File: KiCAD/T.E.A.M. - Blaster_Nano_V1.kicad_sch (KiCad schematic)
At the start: 47 parts, among them J1 USB_C_Receptacle_USB2.0_14P, J2 Conn_01x02, J3 LED, J4 Taster, J5 Speaker, J6 Conn_02x03_Counter_Clockwise, Q1 FS8205A, U1 TP4056-42-ESOP8, U2 DW01A, U3 MT3608, U4 ATMEGA328P-AU, U5 CH340G, U6 DFR0299, Y1 16MHz, Y2 12MHz

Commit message: BOM erstellt und heruntergeladen.
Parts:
- Q1: Availability In Stock -> (none); Package Package -> (none); Price None -> (none)
- U4: Availability In Stock -> (none); Package TQFP-32 Microchip -> (none); Price None -> (none)
- U6: Availability In Stock -> (none); Package None -> (none); Price None -> (none)
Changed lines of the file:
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@@
 			)
 		)
-		(property "Package" "Package"
-			(at 77.47 107.95 0)
-			(hide yes)
-			(show_name no)
-			(do_not_autoplace no)
-			(effects
-				(font
-					(size 1.27 1.27)
-				)
-				(justify bottom)
-			)
-		)
-		(property "Price" "None"
-			(at 77.47 107.95 0)
-			(hide yes)
-			(show_name no)
-			(do_not_autoplace no)
-			(effects
-				(font
-					(size 1.27 1.27)
-				)
-				(justify bottom)
-			)
-		)
 		(property "Check_prices" "https://www.snapeda.com/parts/FS8205A/Fortune+Semiconductor/view-part/?ref=eda"
 			(at 77.47 107.95 0)
@@
 			)
 		)
-		(property "Availability" "In Stock"
-			(at 77.47 107.95 0)
-			(hide yes)
-			(show_name no)
-			(do_not_autoplace no)
-			(effects
-				(font
-					(size 1.27 1.27)
-				)
-				(justify bottom)
-			)
-		)
 		(property "MANUFACTURER" "Fortune Semiconductor"
 			(at 77.47 107.95 0)
@@
 			)
 		)
-		(property "Package" "TQFP-32 Microchip"
-			(at 187.96 55.88 0)
-			(hide yes)
-			(show_name no)
-			(do_not_autoplace no)
-			(effects
-				(font
-					(size 1.27 1.27)
-				)
-				(justify bottom)
-			)
-		)
-		(property "Price" "None"
-			(at 187.96 55.88 0)
-			(hide yes)
-			(show_name no)
-			(do_not_autoplace no)
-			(effects
-				(font
-					(size 1.27 1.27)
-				)
-				(justify bottom)
-			)
-		)
 		(property "Check_prices" "https://www.snapeda.com/parts/ATMEGA328P-AU/Microchip+Technology/view-part/?ref=eda"
 			(at 187.96 55.88 0)
@@
 			)
 		)
-		(property "Availability" "In Stock"
-			(at 187.96 55.88 0)
-			(hide yes)
-			(show_name no)
-			(do_not_autoplace no)
-			(effects
-				(font
-					(size 1.27 1.27)
-				)
-				(justify bottom)
-			)
-		)
 		(property "MANUFACTURER" "Microchip"
 			(at 187.96 55.88 0)
@@
 			)
 		)
-		(property "Package" "None"
-			(at 143.51 135.89 0)
-			(hide yes)
-			(show_name no)
-			(do_not_autoplace no)
-			(effects
-				(font
-					(size 1.27 1.27)
-				)
-				(justify bottom)
-			)
-		)
 		(property "Check_prices" "https://www.snapeda.com/parts/DFR0299/DFRobot/view-part/?ref=eda"
 			(at 143.51 135.89 0)
@@
 			)
 		)
-		(property "Price" "None"
-			(at 143.51 135.89 0)
-			(hide yes)
-			(show_name no)
-			(do_not_autoplace no)
-			(effects
-				(font
-					(size 1.27 1.27)
-				)
-				(justify bottom)
-			)
-		)
 		(property "SnapEDA_Link" "https://www.snapeda.com/parts/DFR0299/DFRobot/view-part/?ref=snap"
 			(at 143.51 135.89 0)
@@
 			(at 143.51 135.89 0)
 			(hide yes)
-			(show_name no)
-			(do_not_autoplace no)
-			(effects
-				(font
-					(size 1.27 1.27)
-				)
-				(justify bottom)
-			)
-		)
-		(property "Availability" "In Stock"
-			(at 143.51 135.89 0)
-			(hide yes)

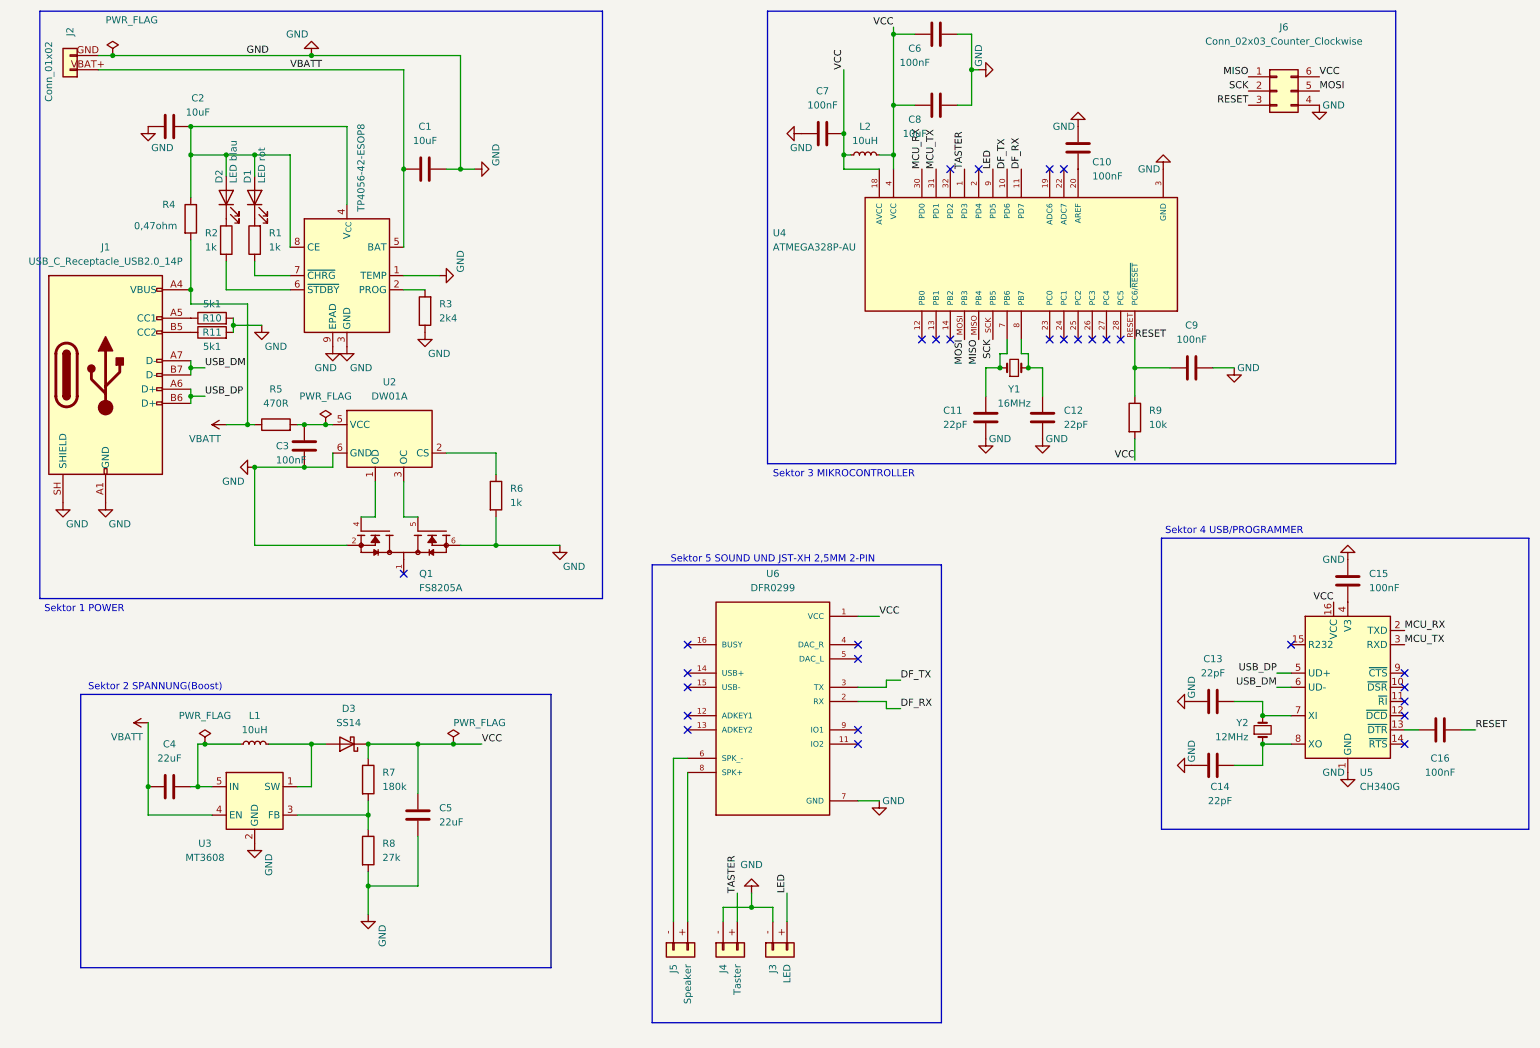
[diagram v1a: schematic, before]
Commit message: Fix schematic pin numbers (J2-J5) and footprint references (Q1, Y1, Y2, U6)
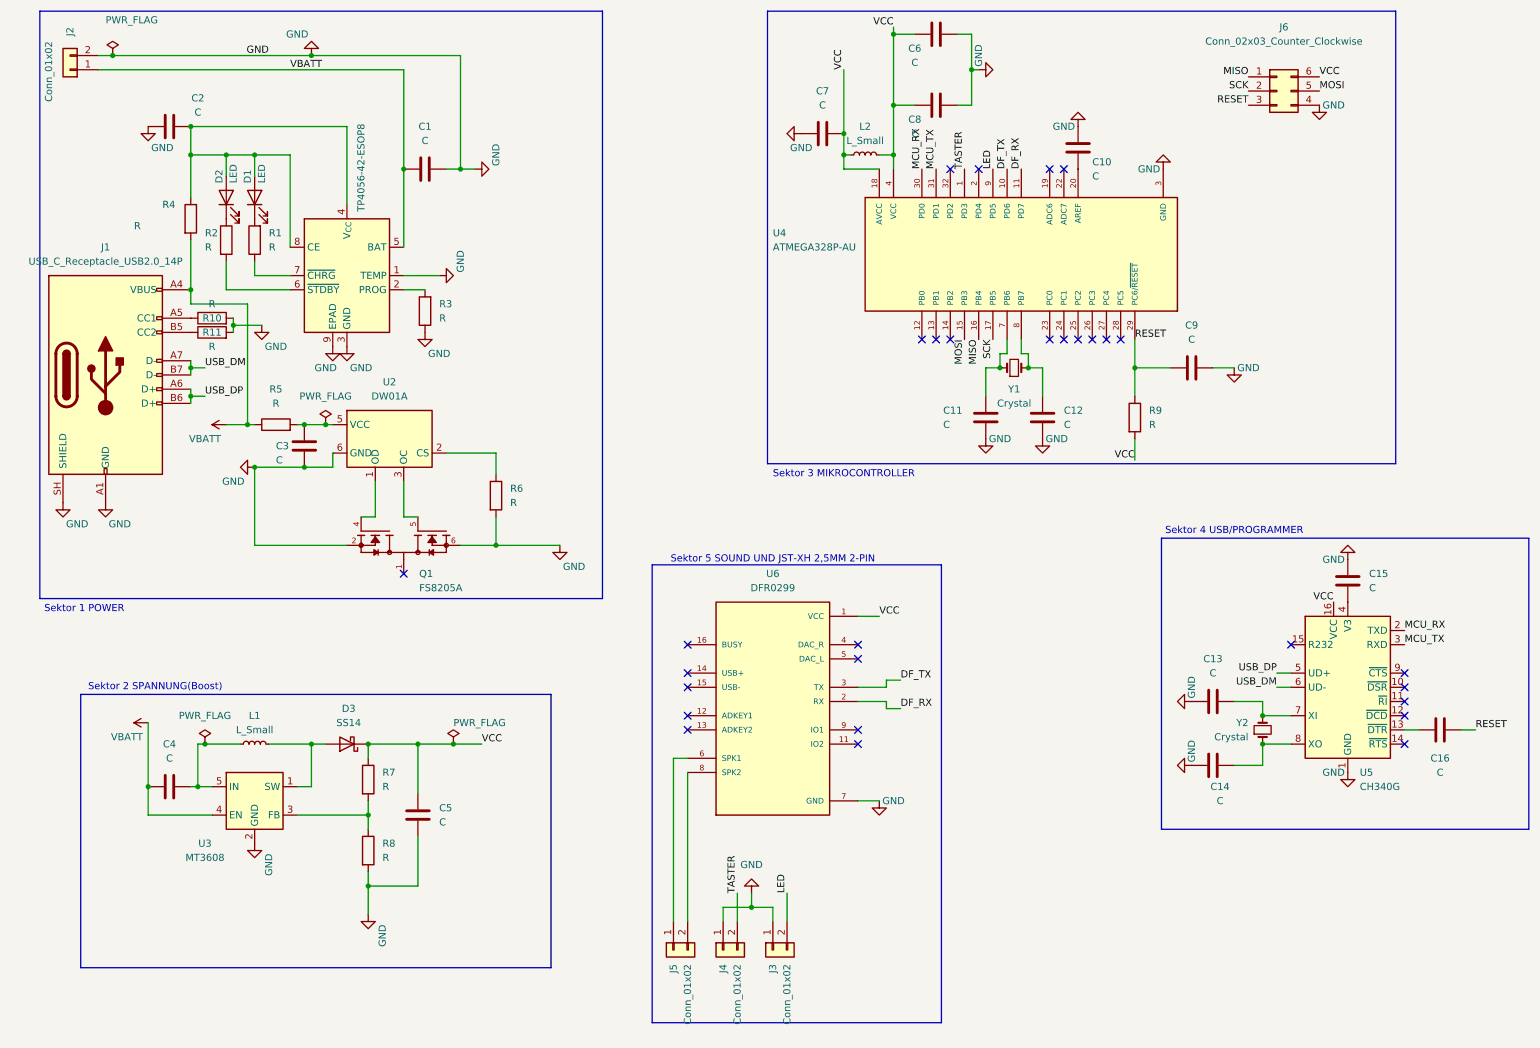
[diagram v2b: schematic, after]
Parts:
- C1, C2, C8: value 10uF -> C
- C10, C15, C16, C3, C6, C7, C9: value 100nF -> C
- C11, C12, C13, C14: value 22pF -> C
- C4, C5: value 22uF -> C
- D1: value LED rot -> LED
- D2: value LED blau -> LED
- J3: value LED -> Conn_01x02
- J4: value Taster -> Conn_01x02
- J5: value Speaker -> Conn_01x02
- L1, L2: value 10uH -> L_Small
- Q1: footprint Package_TO_SOT_SMD:SOT-23-6 -> Package_SO:TSSOP-8_4.4x3mm_P0.65mm
- R1, R2, R6: value 1k -> R
- R10, R11: value 5k1 -> R
- R3: value 2k4 -> R
- R4: value 0,47ohm -> R
- R5: value 470R -> R
- R7: value 180k -> R
- R8: value 27k -> R
- R9: value 10k -> R
- U1: footprint Package_SO:SOIC-8_3.9x4.9mm_P1.27mm -> Package_SO:SOIC-8-1EP_3.9x4.9mm_P1.27mm_EP2.41x3.3mm_ThermalVias
- U4: footprint Package_QFP:TQFP-32_7x7mm_P0.8mm -> ATMEGA328P-AU:QFP80P900X900X120-32N
- Y1: value 16MHz -> Crystal
- Y2: value 12MHz -> Crystal
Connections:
- net GND: now also J2.2 (Pin_2), J3.1 (Pin_1), J4.1 (Pin_1); no longer J2.GND (Pin_2), J3.- (Pin_1), J4.- (Pin_1)
- net LED: now also J3.2 (Pin_2); no longer J3.+ (Pin_2)
- net MISO: now also U4.16 (PB4); no longer U4.MISO (PB4)
- net MOSI: now also U4.15 (PB3); no longer U4.MOSI (PB3)
- net RESET: now also U4.29 (PC6/~{RESET}); no longer U4.RESET (PC6/~{RESET})
- net SCK: now also U4.17 (PB5); no longer U4.SCK (PB5)
- net TASTER: now also J4.2 (Pin_2); no longer J4.+ (Pin_2)
- net VBATT: now also J2.1 (Pin_1); no longer J2.VBAT+ (Pin_1)
- net at U6.8 (SPK2): now also J5.2 (Pin_2); no longer J5.+ (Pin_2)
- net at U6.6 (SPK1): now also J5.1 (Pin_1); no longer J5.- (Pin_1)
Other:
- moved on the sheet: J2

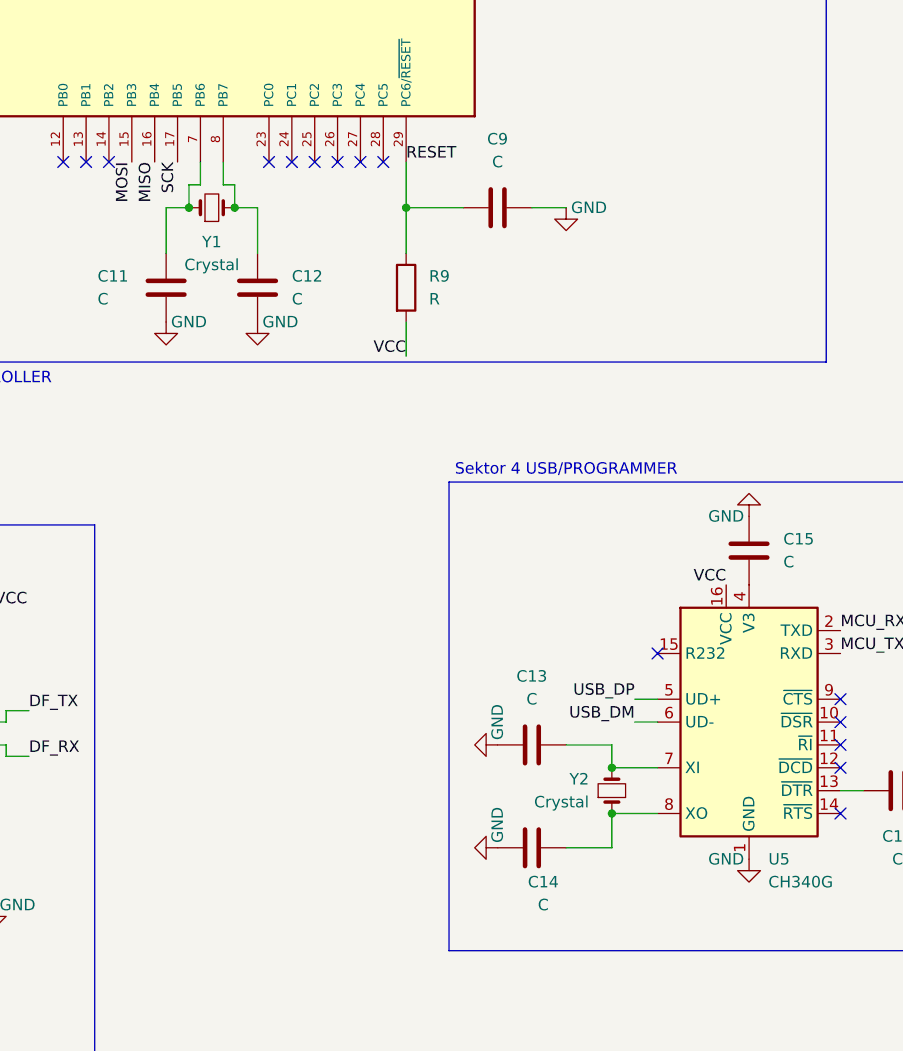
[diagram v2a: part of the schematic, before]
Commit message: Add Crystal_GND31 symbol and connect crystal shield to GND
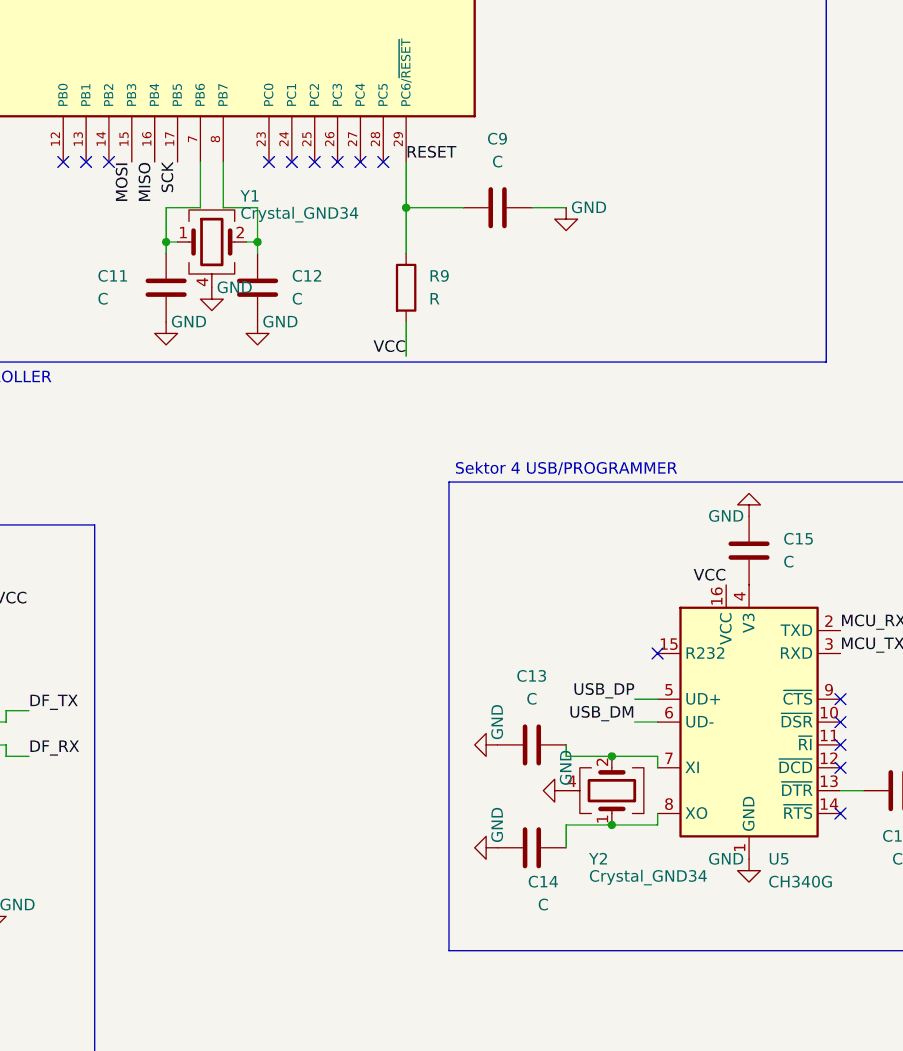
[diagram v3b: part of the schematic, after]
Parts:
- Y1, Y2: value Crystal -> Crystal_GND34; symbol SparkFun-Clock:Crystal -> TEAM_Custom:Crystal_GND34
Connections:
- net GND: now also Y1.3 (G), Y1.4 (G), Y2.3 (G), Y2.4 (G)
